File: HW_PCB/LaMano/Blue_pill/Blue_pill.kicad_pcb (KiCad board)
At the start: 2 copper layers, 41.1 x 42.8 mm, 28 parts, among them J1 V_Battery, J2 STLINK, J5 MPU6050, J6 NRF24, SW1 SW_DPST_x2, SW2 SW_DPST_x2, U1 STM32F103C8Tx, U2 AMS1117-3.3, X1 Crystal

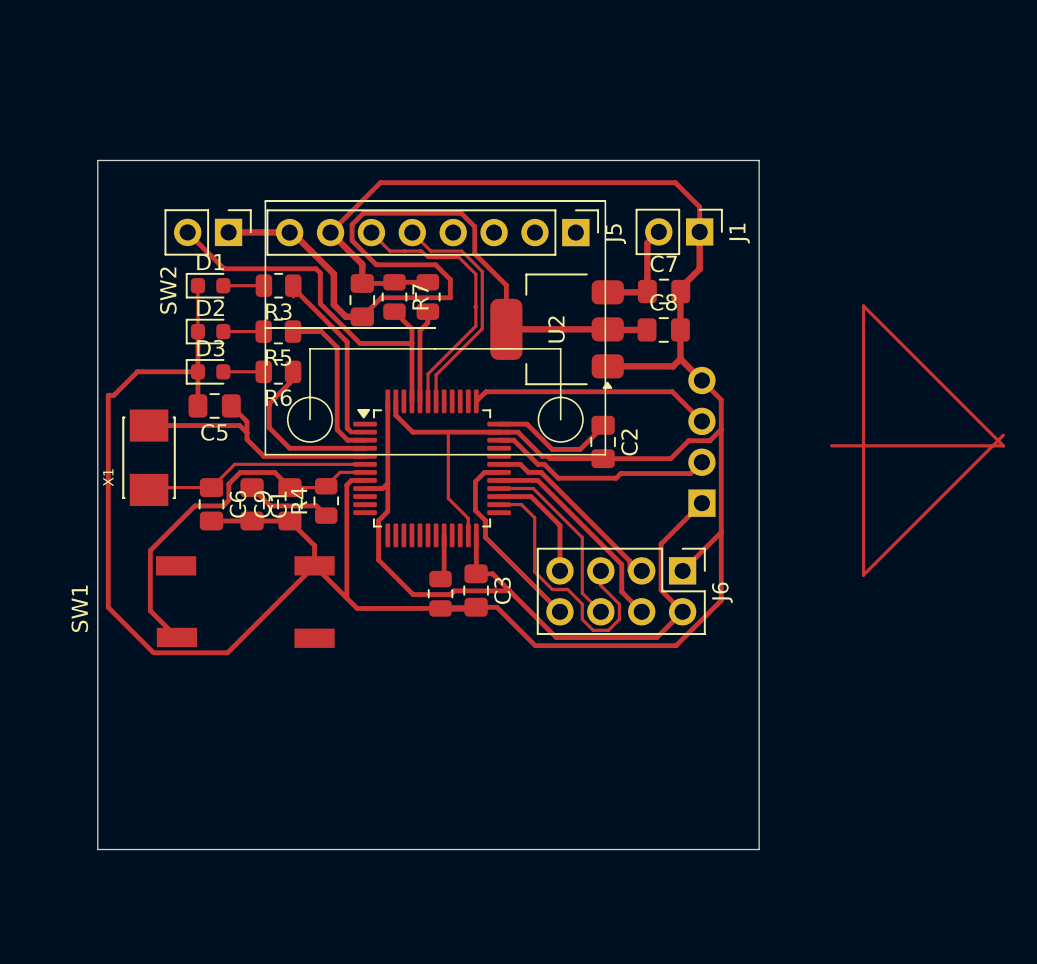
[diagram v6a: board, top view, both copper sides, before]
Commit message: Added bottom layer, pending to aprove
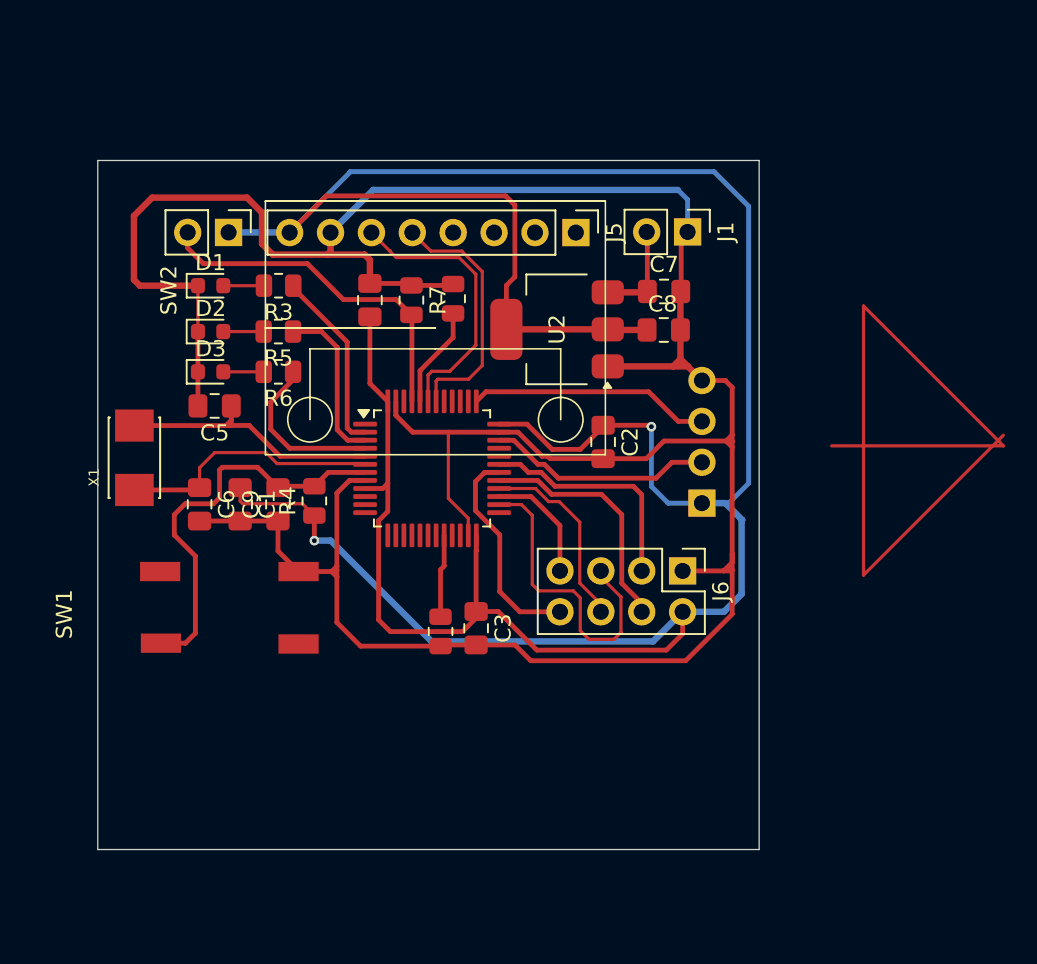
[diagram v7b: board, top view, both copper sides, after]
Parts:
- moved C3 2.34 mm to (62.1, 71.5)
- moved R1 2.34 mm to (59.9, 71.7)
- moved R2 1.57 mm to (60.7, 51.0)
- moved R7 1.07 mm to (58.1, 51.1)
- moved SW1 1.05 mm to (37.0, 70.6)
- moved X1 0.91 mm to (40.9, 60.9)
- moved J1 0.75 mm to (75.3, 46.9)
- moved C1 0.74 mm to (47.5, 63.8)
- moved C9 0.74 mm to (49.8, 63.8)
- moved R4 0.74 mm to (52.1, 63.6)
- moved C6 0.74 mm to (45.0, 63.8)
- moved C4 0.47 mm to (55.5, 51.1)
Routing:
- net VCC: track 111.0 -> 200.1 mm, vias 0 -> 2
- net NRST: track 22.8 -> 25.4 mm
- net CE: track 12.0 -> 14.4 mm
- net Net-(U1-PB2): track 2.81 -> 5.15 mm
- net SCK: track 17.0 -> 19.3 mm
- net OSC_OUT: track 14.3 -> 16.3 mm
- net SW_LUZ: track 23.9 -> 22.0 mm
- net CSN: track 13.2 -> 15.1 mm
- net IRQ: track 12.7 -> 14.2 mm
- net SDA: track 14.6 -> 15.7 mm
- net GND: track 185.2 -> 184.2 mm
- net RED: track 12.1 -> 11.4 mm
- net SCL: track 16.7 -> 17.3 mm
- net Net-(U1-BOOT0): track 5.78 -> 6.32 mm

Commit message: Increased the vein sizes
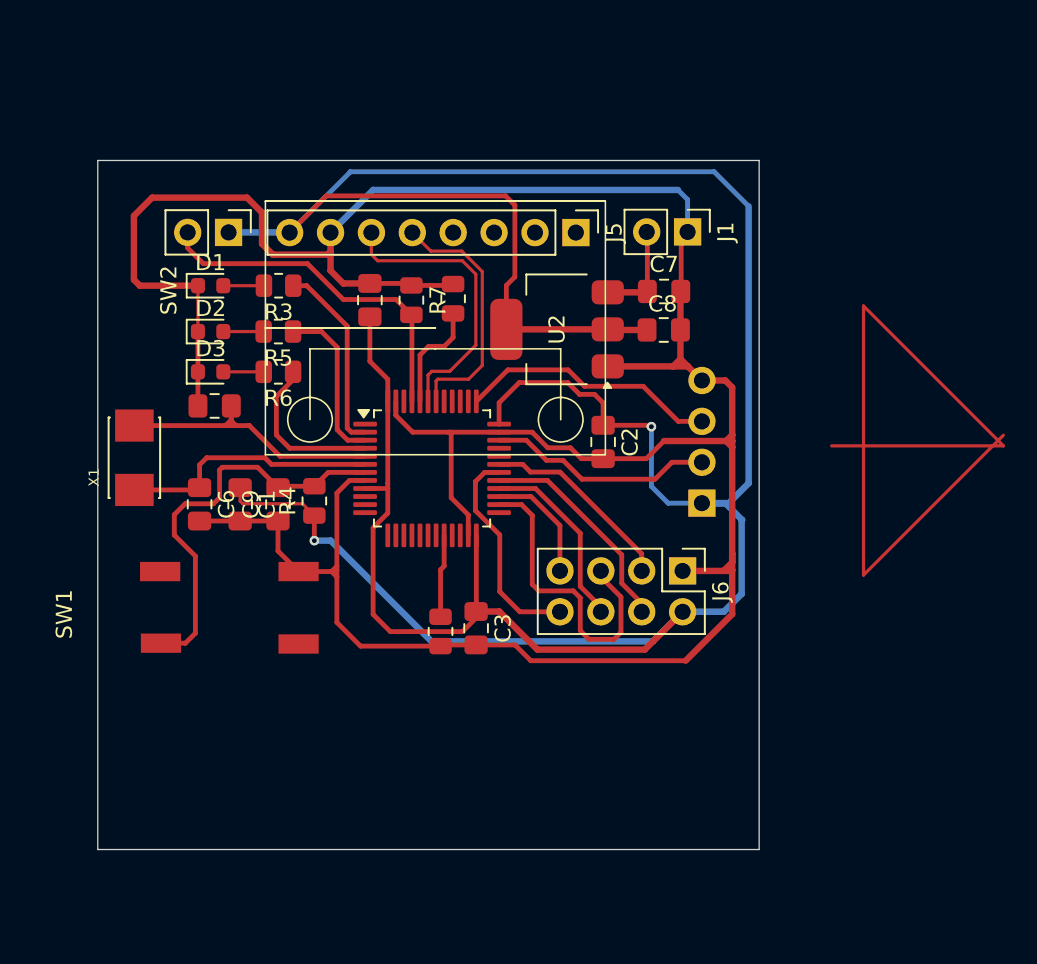
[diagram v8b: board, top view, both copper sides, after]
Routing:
- net CE: track 14.4 -> 12.2 mm
- net VCC: track 200.1 -> 201.9 mm
- net CSN: track 15.1 -> 13.6 mm
- net SWCLK: track 15.0 -> 16.2 mm
- net SCL: track 17.3 -> 18.1 mm
- net Net-(U1-BOOT0): track 6.32 -> 6.88 mm
- net OSC_IN: track 16.8 -> 17.4 mm
